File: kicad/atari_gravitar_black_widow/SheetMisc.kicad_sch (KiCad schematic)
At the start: 4 parts, among them J17 cat_box_con, J19 J19, J20 J20

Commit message: Fixed most errors
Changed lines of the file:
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@@
   (no_connect (at 147.32 76.2))
   (no_connect (at 115.57 78.74))
+  (wire (pts (xy 69.469 110.49) (xy 72.771 110.49))
+    (stroke (width 0) (type default) (color 0 0 0 0))
+  )
+  (wire (pts (xy 42.926 117.348) (xy 42.926 119.507))
+    (stroke (width 0) (type default) (color 0 0 0 0))
+  )
   (wire (pts (xy 115.57 71.12) (xy 111.76 71.12))
     (stroke (width 0) (type default) (color 0 0 0 0))
   )
   (wire (pts (xy 115.57 66.04) (xy 111.76 66.04))
+    (stroke (width 0) (type default) (color 0 0 0 0))
+  )
+  (wire (pts (xy 44.45 104.394) (xy 48.26 104.394))
+    (stroke (width 0) (type default) (color 0 0 0 0))
+  )
+  (wire (pts (xy 40.513 95.758) (xy 44.45 95.758))
+    (stroke (width 0) (type default) (color 0 0 0 0))
+  )
+  (wire (pts (xy 69.088 94.996) (xy 72.39 94.996))
     (stroke (width 0) (type default) (color 0 0 0 0))
   )
@@
       (effects (font (size 1.27 1.27)) hide)
     )
+    (pin "1")
+  )
+  (symbol (lib_id "power:-24V") (at 69.469 110.49 90) (unit 1)
+    (in_bom yes) (on_board yes)
+    (property "Reference" "#PWR0536" (id 0) (at 66.929 110.49 0)
+      (effects (font (size 1.27 1.27)) hide)
+    )
+    (property "Value" "-24V" (id 1) (at 66.2178 110.109 90)
+      (effects (font (size 1.27 1.27)) (justify left))
+    )
+    (property "Footprint" "" (id 2) (at 69.469 110.49 0)
+      (effects (font (size 1.27 1.27)) hide)
+    )
+    (property "Datasheet" "" (id 3) (at 69.469 110.49 0)
+      (effects (font (size 1.27 1.27)) hide)
+    )
+    (pin "1")
+  )
+  (symbol (lib_id "power:PWR_FLAG") (at 42.926 117.348 0) (unit 1)
+    (in_bom yes) (on_board yes) (fields_autoplaced)
+    (property "Reference" "#FLG0103" (id 0) (at 42.926 115.443 0)
+      (effects (font (size 1.27 1.27)) hide)
+    )
+    (property "Value" "PWR_FLAG" (id 1) (at 42.926 113.7435 0))
+    (property "Footprint" "" (id 2) (at 42.926 117.348 0)
+      (effects (font (size 1.27 1.27)) hide)
+    )
+    (property "Datasheet" "~" (id 3) (at 42.926 117.348 0)
+      (effects (font (size 1.27 1.27)) hide)
+    )
+    (pin "1")
+  )
+  (symbol (lib_id "power:PWR_FLAG") (at 44.45 95.758 0) (unit 1)
+    (in_bom yes) (on_board yes) (fields_autoplaced)
+    (property "Reference" "#FLG0101" (id 0) (at 44.45 93.853 0)
+      (effects (font (size 1.27 1.27)) hide)
+    )
+    (property "Value" "PWR_FLAG" (id 1) (at 44.45 92.1535 0))
+    (property "Footprint" "" (id 2) (at 44.45 95.758 0)
+      (effects (font (size 1.27 1.27)) hide)
+    )
+    (property "Datasheet" "~" (id 3) (at 44.45 95.758 0)
+      (effects (font (size 1.27 1.27)) hide)
+    )
+    (pin "1")
+  )
+  (symbol (lib_id "power:+5V") (at 44.45 104.394 90) (unit 1)
+    (in_bom yes) (on_board yes)
+    (property "Reference" "#PWR0533" (id 0) (at 48.26 104.394 0)
+      (effects (font (size 1.27 1.27)) hide)
+    )
+    (property "Value" "+5V" (id 1) (at 41.1988 104.013 90)
+      (effects (font (size 1.27 1.27)) (justify left))
+    )
+    (property "Footprint" "" (id 2) (at 44.45 104.394 0)
+      (effects (font (size 1.27 1.27)) hide)
+    )
+    (property "Datasheet" "" (id 3) (at 44.45 104.394 0)
+      (effects (font (size 1.27 1.27)) hide)
+    )
+    (pin "1")
+  )
+  (symbol (lib_id "power:PWR_FLAG") (at 48.26 104.394 0) (unit 1)
+    (in_bom yes) (on_board yes) (fields_autoplaced)
+    (property "Reference" "#FLG0102" (id 0) (at 48.26 102.489 0)
+      (effects (font (size 1.27 1.27)) hide)
+    )
+    (property "Value" "PWR_FLAG" (id 1) (at 48.26 100.7895 0))
+    (property "Footprint" "" (id 2) (at 48.26 104.394 0)
+      (effects (font (size 1.27 1.27)) hide)
+    )
+    (property "Datasheet" "~" (id 3) (at 48.26 104.394 0)
+      (effects (font (size 1.27 1.27)) hide)
+    )
+    (pin "1")
+  )
+  (symbol (lib_id "power:+10V") (at 40.513 95.758 90) (unit 1)
+    (in_bom yes) (on_board yes)
+    (property "Reference" "#PWR0532" (id 0) (at 44.323 95.758 0)
+      (effects (font (size 1.27 1.27)) hide)
+    )
+    (property "Value" "+10V" (id 1) (at 37.2618 95.377 90)
+      (effects (font (size 1.27 1.27)) (justify left))
+    )
+    (property "Footprint" "" (id 2) (at 40.513 95.758 0)
+      (effects (font (size 1.27 1.27)) hide)
+    )
+    (property "Datasheet" "" (id 3) (at 40.513 95.758 0)
+      (effects (font (size 1.27 1.27)) hide)
+    )
+    (pin "1")
+  )
+  (symbol (lib_id "power:PWR_FLAG") (at 72.39 94.996 0) (unit 1)
+    (in_bom yes) (on_board yes) (fields_autoplaced)
+    (property "Reference" "#FLG0104" (id 0) (at 72.39 93.091 0)
+      (effects (font (size 1.27 1.27)) hide)
+    )
+    (property "Value" "PWR_FLAG" (id 1) (at 72.39 91.3915 0))
+    (property "Footprint" "" (id 2) (at 72.39 94.996 0)
+      (effects (font (size 1.27 1.27)) hide)
+    )
+    (property "Datasheet" "~" (id 3) (at 72.39 94.996 0)
+      (effects (font (size 1.27 1.27)) hide)
+    )
+    (pin "1")
+  )
+  (symbol (lib_id "power:GND") (at 42.926 119.507 0) (unit 1)
+    (in_bom yes) (on_board yes) (fields_autoplaced)
+    (property "Reference" "#PWR0534" (id 0) (at 42.926 125.857 0)
+      (effects (font (size 1.27 1.27)) hide)
+    )
+    (property "Value" "GND" (id 1) (at 42.926 124.0695 0))
+    (property "Footprint" "" (id 2) (at 42.926 119.507 0)
+      (effects (font (size 1.27 1.27)) hide)
+    )
+    (property "Datasheet" "" (id 3) (at 42.926 119.507 0)
+      (effects (font (size 1.27 1.27)) hide)
+    )
+    (pin "1")
+  )
+  (symbol (lib_id "power:PWR_FLAG") (at 72.771 110.49 0) (unit 1)
+    (in_bom yes) (on_board yes) (fields_autoplaced)
+    (property "Reference" "#FLG0105" (id 0) (at 72.771 108.585 0)
+      (effects (font (size 1.27 1.27)) hide)
+    )
+    (property "Value" "PWR_FLAG" (id 1) (at 72.771 106.8855 0))
+    (property "Footprint" "" (id 2) (at 72.771 110.49 0)
+      (effects (font (size 1.27 1.27)) hide)
+    )
+    (property "Datasheet" "~" (id 3) (at 72.771 110.49 0)
+      (effects (font (size 1.27 1.27)) hide)
+    )
+    (pin "1")
+  )
+  (symbol (lib_id "power:+24V") (at 69.088 94.996 90) (unit 1)
+    (in_bom yes) (on_board yes)
+    (property "Reference" "#PWR0535" (id 0) (at 72.898 94.996 0)
+      (effects (font (size 1.27 1.27)) hide)
+    )
+    (property "Value" "+24V" (id 1) (at 65.8368 94.615 90)
+      (effects (font (size 1.27 1.27)) (justify left))
+    )
+    (property "Footprint" "" (id 2) (at 69.088 94.996 0)
+      (effects (font (size 1.27 1.27)) hide)
+    )
+    (property "Datasheet" "" (id 3) (at 69.088 94.996 0)
+      (effects (font (size 1.27 1.27)) hide)
+    )

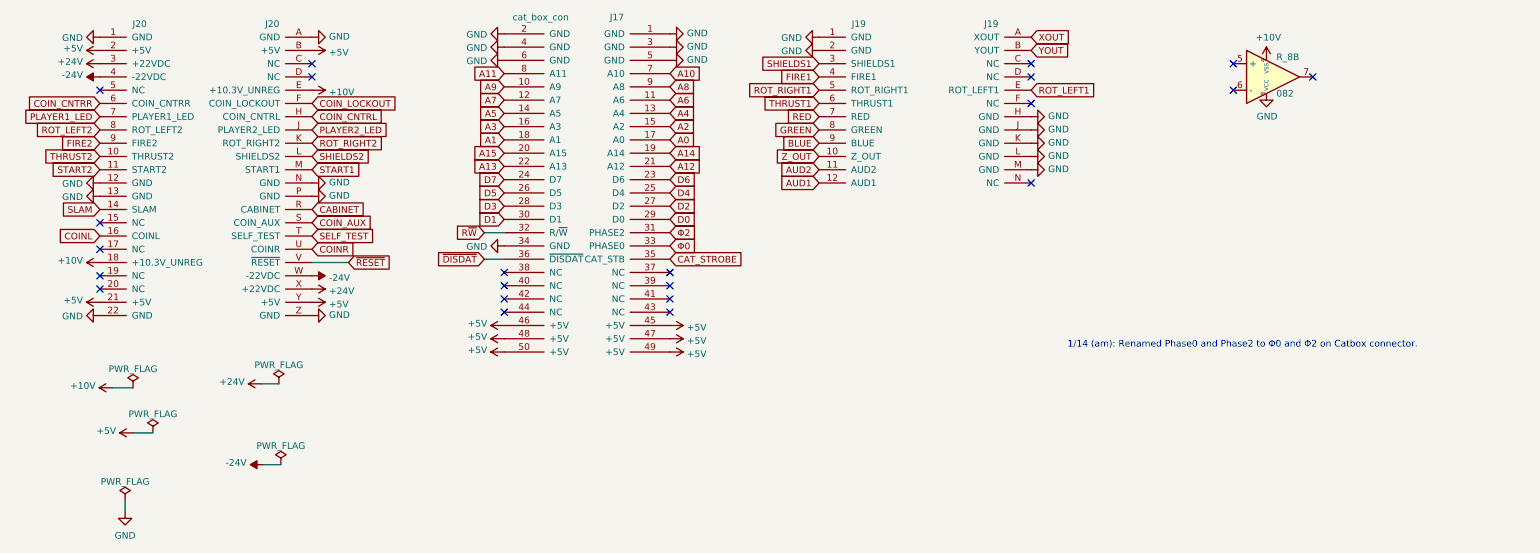
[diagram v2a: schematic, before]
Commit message: Worked on removing the warnings
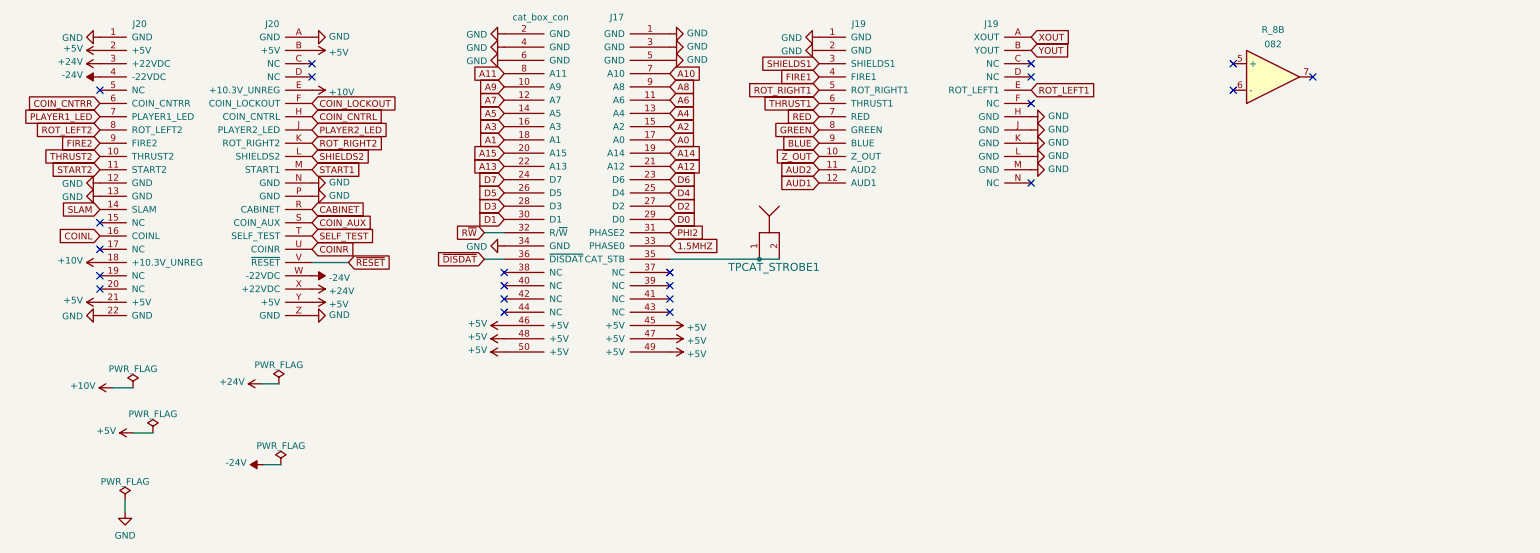
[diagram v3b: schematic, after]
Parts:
- added TPCAT_STROBE1: TP, symbol atari_grav_bw:TP
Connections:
- net +10V: no longer R_8.4 (VSS)
- net GND: no longer R_8.8 (VCC)
- net CAT_STROBE: no longer names the net of J17.35 (CAT_STB)
- net CAT_STROBE: now also TPCAT_STROBE1.1, TPCAT_STROBE1.2
- net Φ0 renamed 1.5MHZ
- net Φ2 renamed PHI2
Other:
- note removed: "1/14 (am): Renamed Phase0 and Phase2 to Φ0 and Φ2 on Catbox connector."
